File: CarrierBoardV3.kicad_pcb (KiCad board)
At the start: 4 copper layers, 92 x 96 mm, 86 parts, among them J1 USB_B_Micro, J10 Conn_02x26_Odd_Even, J2 Conn_02x09_Odd_Even, J3 Barrel_Jack, J4 TX2iConnctor, J5 Conn_01x03_Male, J6 Conn_02x04_Odd_Even, J7 Conn_02x03_Odd_Even, J8 Conn_02x26_Odd_Even, J9 Conn_01x03_Male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

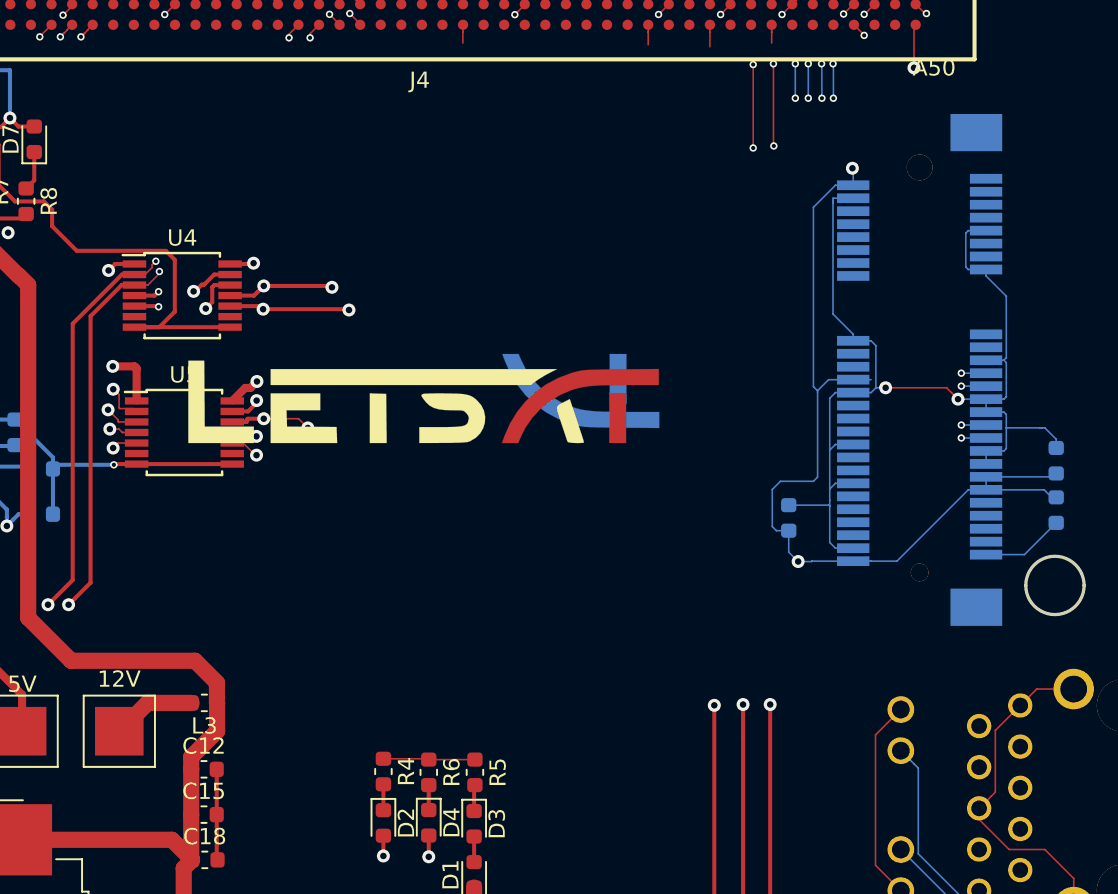
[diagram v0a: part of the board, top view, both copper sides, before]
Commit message: Sata mounting holes added, all routes connected and finished as far as I know, waiting for Prabodh to have a final look over
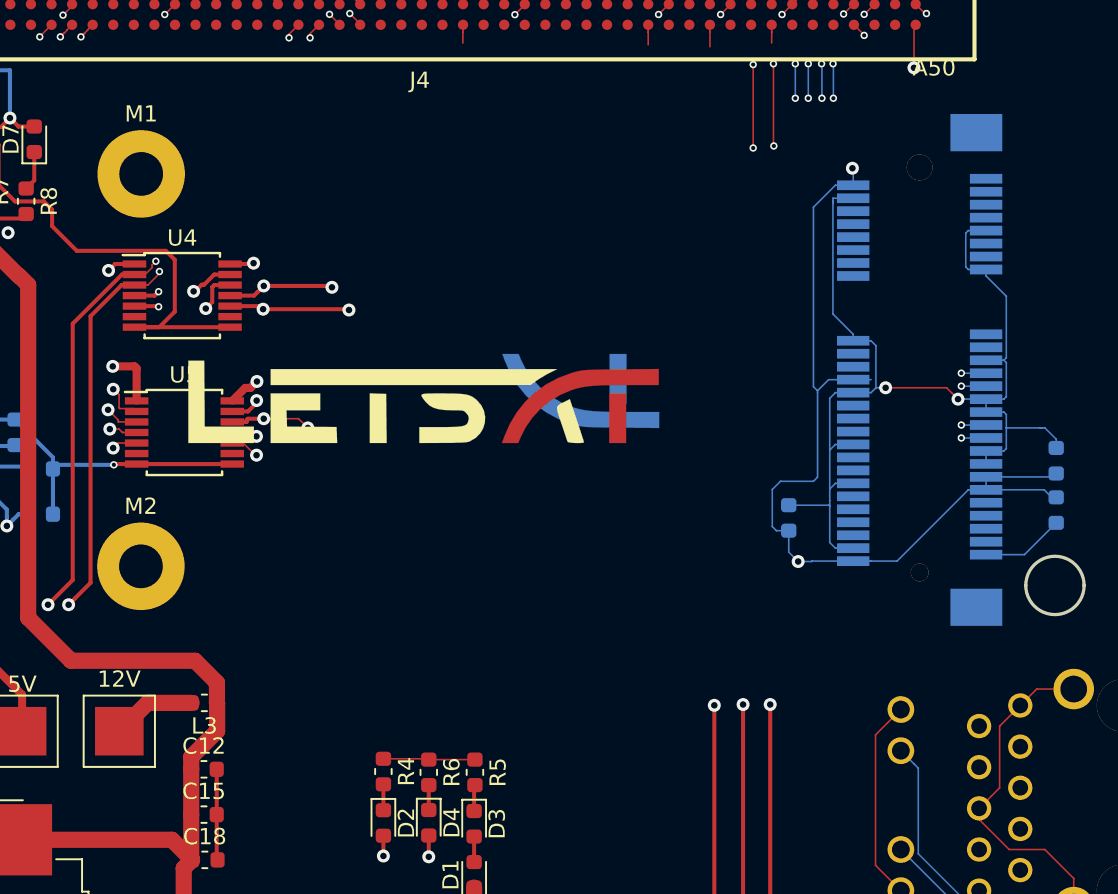
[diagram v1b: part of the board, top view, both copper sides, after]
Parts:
- added M1: MountingHole_2.7mm_M2.5_Pad, MountingHole:MountingHole_2.7mm_M2.5_Pad, F.Cu at (127.9, 87.2)
- added M2: MountingHole_2.7mm_M2.5_Pad, MountingHole:MountingHole_2.7mm_M2.5_Pad, F.Cu at (127.9, 111.4)

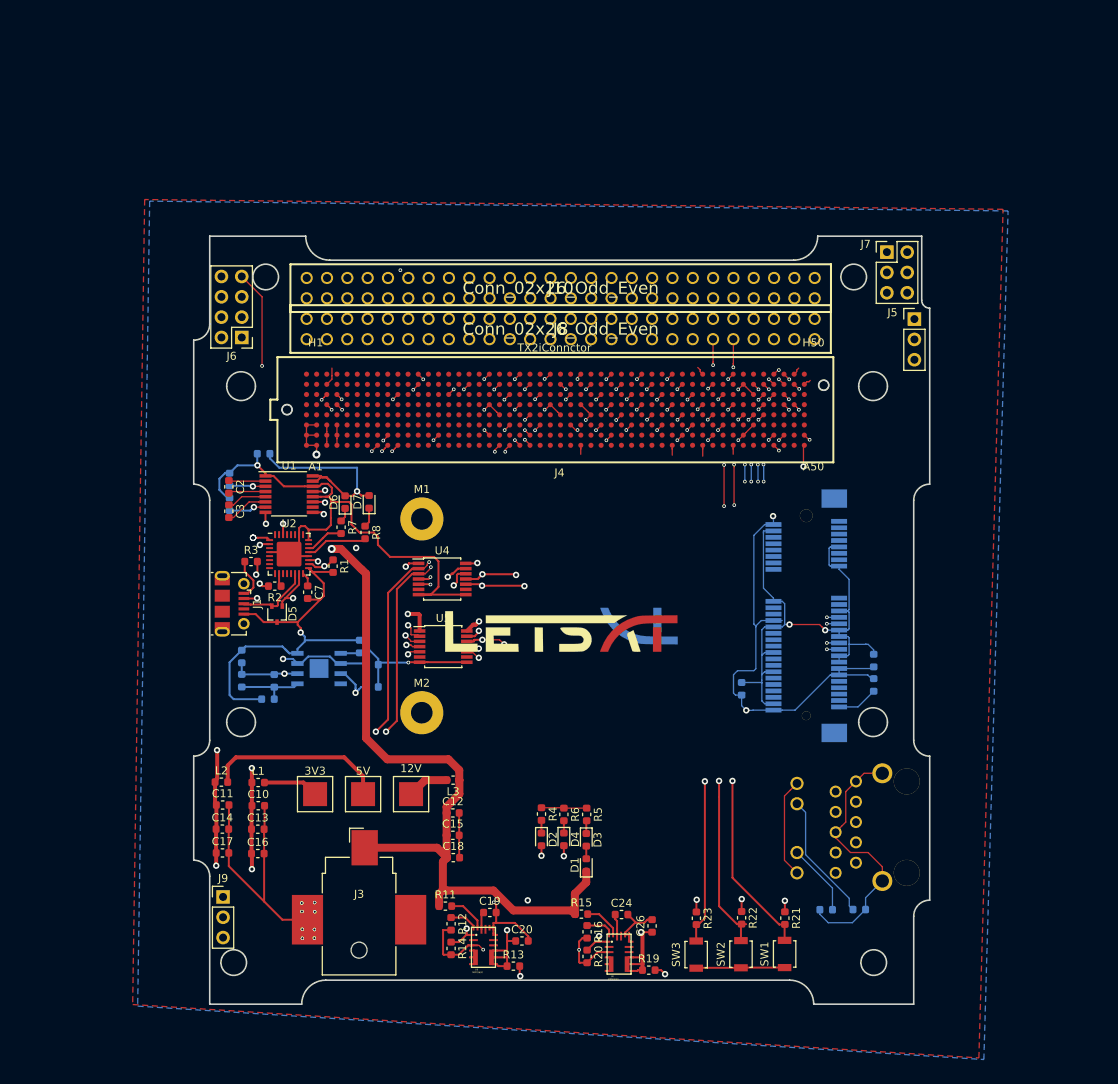
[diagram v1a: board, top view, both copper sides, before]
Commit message: All trace edits complete and re routes
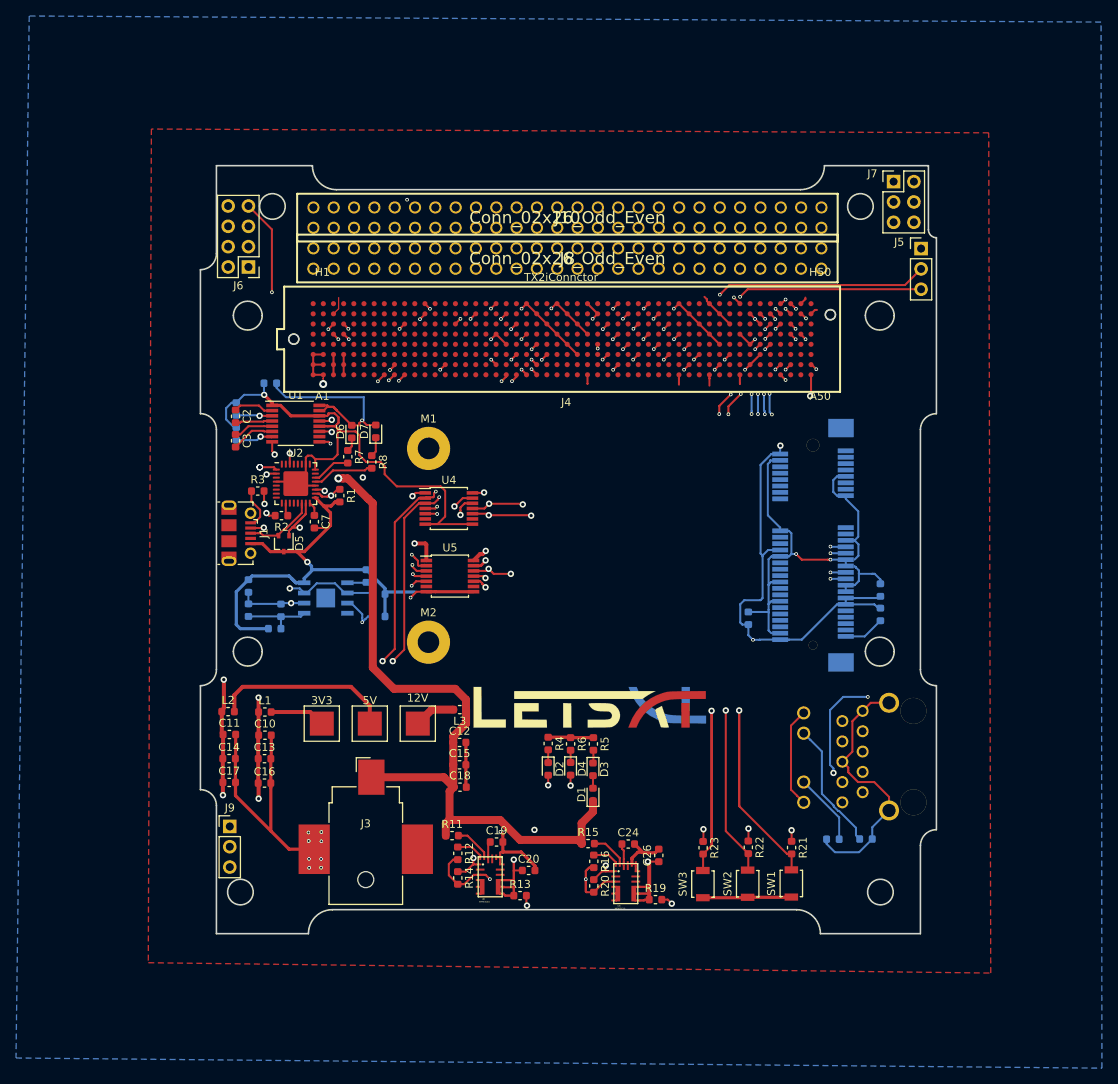
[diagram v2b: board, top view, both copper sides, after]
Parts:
- moved G*** 10.5 mm to (149.1, 110.5)
- moved G*** 10.1 mm to (149.0, 111.0)
- moved C16 8.85 mm to (108.3, 120.2)
- moved C20 8.85 mm to (141.3, 131.1)
- moved R23 8.85 mm to (163.1, 128.3)
- moved R9 8.85 mm to (179.3, 127.2)
- moved SW1 8.85 mm to (174.1, 132.8)
- moved SW2 8.85 mm to (168.6, 132.8)
- moved J6 8.85 mm to (106.2, 55.7)
- moved M1 8.85 mm to (128.8, 78.4)
- moved 12V 8.85 mm to (127.4, 112.8)
- moved 3V3 8.85 mm to (115.4, 112.8)
- moved 5V 8.85 mm to (121.4, 112.8)
- moved C1 8.85 mm to (109.0, 70.2)
- moved C10 8.85 mm to (108.3, 114.2)
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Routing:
- net TX2i_3V3: track 323.7 -> 364.6 mm
- net TX2i_5V: track 307.0 -> 340.2 mm
- net WAKE1n: track 70.5 -> 94.3 mm
- net GBE_CTREF(GND): track 405.9 -> 429.6 mm, vias 74 -> 60
- net PWRBTNn: track 75.2 -> 91.3 mm
- net I2C_DAT: track 39.4 -> 24.1 mm
- net SATA_RX+: track 41.5 -> 55.5 mm
- net SATA_RX-: track 40.8 -> 52.3 mm
- net GBE_MDI0-: track 96.1 -> 87.9 mm
- net TX2i_1.8V: track 44.3 -> 50.7 mm
- net Net-(D5-Pad1): track 12.1 -> 16.6 mm
- net SYS_RESETn: track 71.5 -> 75.8 mm
- net SPI0_MI: track 39.1 -> 35.5 mm
- net SPI0_MOSI: track 93.7 -> 90.5 mm
- net SPI0_CS0#: track 93.1 -> 90.4 mm
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
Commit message: PCB touch up
Added shunts for SWs and fixed some trace shorts
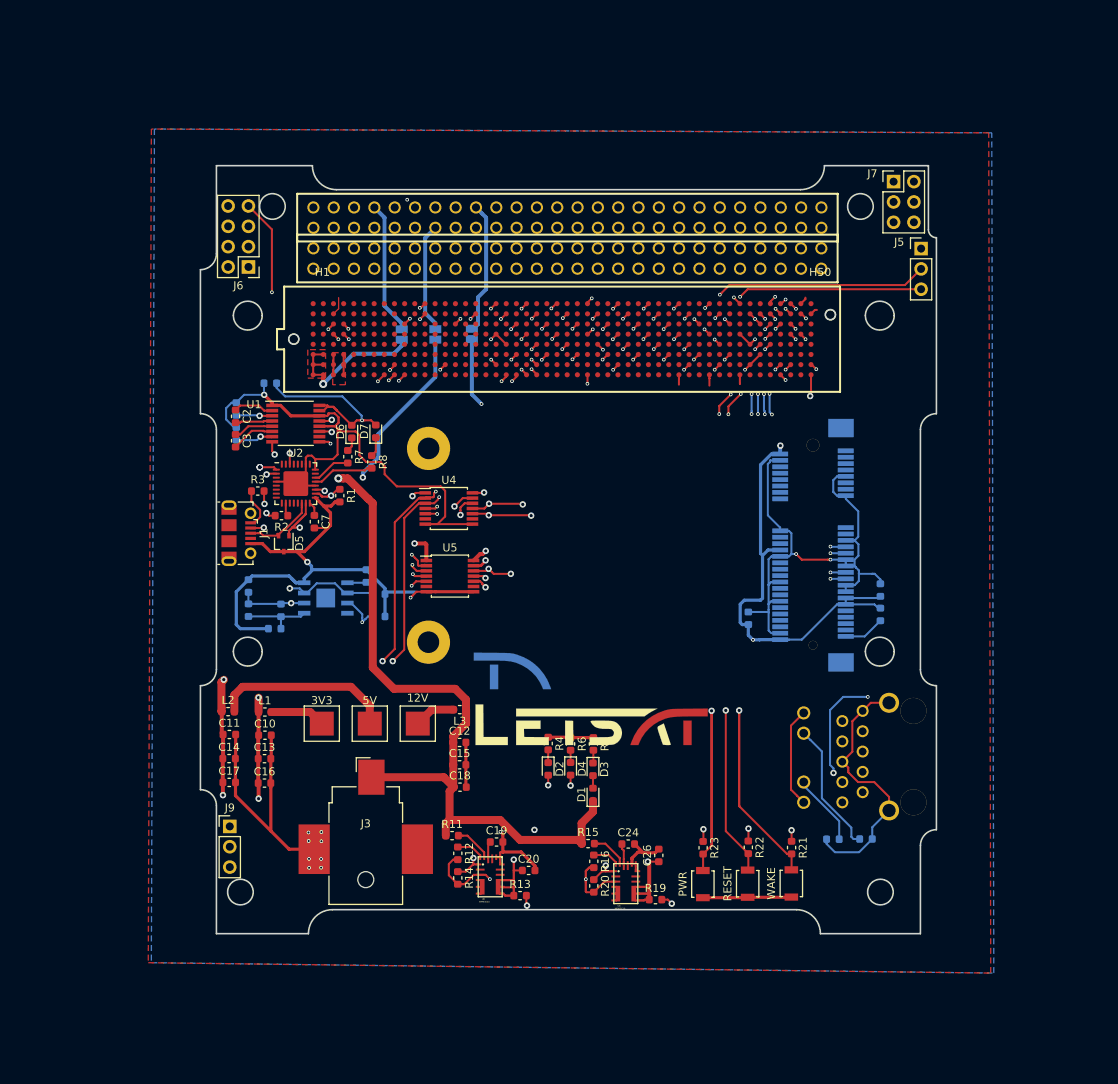
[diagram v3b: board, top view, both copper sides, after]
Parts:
- added J11: SW1-12V_SHUNT, Jumper:SolderJumper-2_P1.3mm_Open_Pad1.0x1.5mm, B.Cu at (125.4, 64.2)
- added J12: SW8-3V3_SHUNT, Jumper:SolderJumper-2_P1.3mm_Open_Pad1.0x1.5mm, B.Cu at (134.2, 64.1)
- added J13: SW5-5V_SHUNT, Jumper:SolderJumper-2_P1.3mm_Open_Pad1.0x1.5mm, B.Cu at (129.6, 64.1)
- moved G*** 4.35 mm to (148.8, 106.2), turned to 180 degrees
- moved G*** 2.20 mm to (149.3, 113.2)
- renumbered SW3 to PWR, SW2 to RESET, SW1 to WAKE
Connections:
- J10 pad 10: TX2i_5V -> SW2
- J10 pad 12: TX2i_3V3 -> SW4
- J10 pad 8: TX2i_12V -> SW1
- J4 pad H46: TX2i_GND -> GBE_CTREF(GND)
- J8 pad 32: TX2i_5V -> USB_CHG5V
- L2 pad 2: Net-(L2-Pad2) -> Net-(5V1-Pad1)
- L3 pad 2: Net-(L3-Pad2) -> Net-(12V1-Pad1)
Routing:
- net TX2i_5V: track 340.2 -> 296.6 mm
- net TX2i_12V: track 149.8 -> 127.1 mm
- net TX2i_3V3: track 364.6 -> 381.4 mm, vias 8 -> 9
- net SW1: track 0.00 -> 16.7 mm
- net SW8: track 0.00 -> 16.5 mm
- net SW5: track 0.00 -> 13.7 mm
- net GNDA: track 32.3 -> 20.3 mm
- net GBE_CTREF(GND): track 429.6 -> 419.2 mm, vias 60 -> 78
- net UART0_TX: track 89.9 -> 90.5 mm
- added copper zone on F.Cu, net TX2i_12V
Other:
- board text added: "SW1_SHUNT12V"
- board text added: "SW5_SHUNT5V"
- board text added: "SW8_SHUNT3V3"

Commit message: fixed stuff
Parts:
- moved G*** 6.80 mm to (149.1, 106.4)
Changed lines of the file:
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@@
   )
   (setup
-    (last_trace_width 0.1)
+    (last_trace_width 0.25)
     (user_trace_width 0.1)
     (user_trace_width 0.15)
@@
   )
   (module CarrierBoardV3:LetSat_Logo_Front (layer F.Cu)
-    (at 149.2885 113.157)
+    (at 149.098 106.3625)
     (fp_text reference G*** (at 0 0) (layer F.SilkS) hide
       (effects (font (size 1.524 1.524) (thickness 0.3)))
@@
     (pad A1 smd circle (at 31.115 -4.445 180) (size 0.635 0.635) (layers F.Cu F.Paste F.Mask)
       (net 8 TX2i_12V))
+    (model ${KIPRJMOD}/SEAM-50-02.0-S-08-2-A-K-TR.stp
+      (offset (xyz 0 0 1.5))
+      (scale (xyz 1 1 1))
+      (rotate (xyz -90 0 0))
+    )
   )
   (module LED_SMD:LED_0603_1608Metric (layer F.Cu)
@@
   (segment (start 165.1682 50.8062) (end 166.24583 50.8062) (width 0.254) (layer In2.Cu) (net 418))
   (segment (start 170.2482 48.2662) (end 170.2482 50.8062) (width 1) (layer In1.Cu) (net 419))
-  (segment (start 115.4132 112.7862) (end 113.9632 111.3362) (width 1) (layer F.Cu) (net 512))
-  (segment (start 109.0882 111.3362) (end 113.9632 111.3362) (width 1) (layer F.Cu) (net 512))
   (segment (start 104.4882 109.2112) (end 104.4882 111.2862) (width 1) (layer F.Cu) (net 424))
   (segment (start 105.5132 108.1862) (end 104.4882 109.2112) (width 1) (layer F.Cu) (net 424))
@@
   (segment (start 106.2482 99.3902) (end 110.2867 99.3902) (width 0.254) (layer B.Cu) (net 510))
   (segment (start 110.3122 99.4157) (end 110.3122 100.9142) (width 0.254) (layer B.Cu) (net 510))
+  (segment (start 115.4132 112.7862) (end 113.9632 111.3362) (width 1) (layer F.Cu) (net 512))
+  (segment (start 109.0882 111.3362) (end 113.9632 111.3362) (width 1) (layer F.Cu) (net 512))
   (segment (start 125.4125 62.75) (end 123.2535 60.591) (width 0.5) (layer B.Cu) (net 516))
   (segment (start 125.4125 63.5) (end 125.4125 62.75) (width 0.5) (layer B.Cu) (net 516))
